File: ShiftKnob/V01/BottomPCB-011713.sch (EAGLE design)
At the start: 38 parts, among them IC2 7805DT, Q1 16MHz, Q2 MOSFET-NCHANNELSMD, Q3 MOSFET-NCHANNELSMD, Q4 MOSFET-NCHANNELSMD, Q5 MOSFET-NCHANNELSMD, Q6 MOSFET-NCHANNELSMD, U1 ATMEGA328

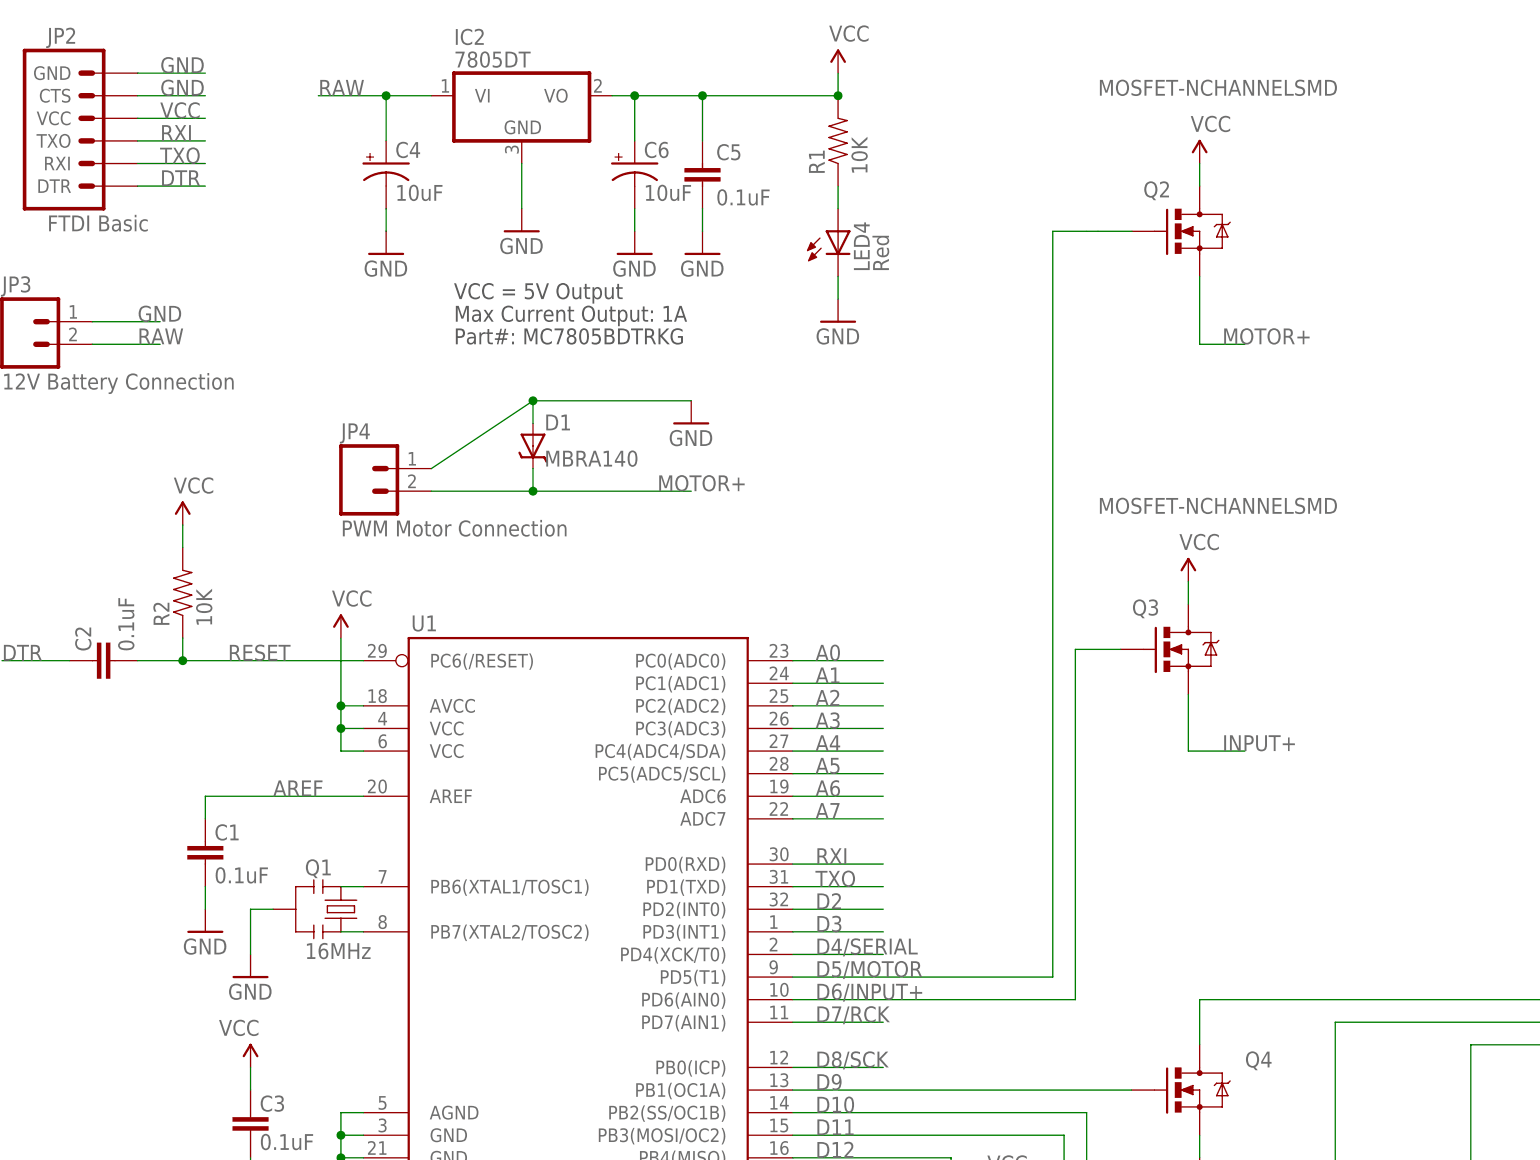
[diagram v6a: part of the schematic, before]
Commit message: add schottky diode to hand usb power auto selection
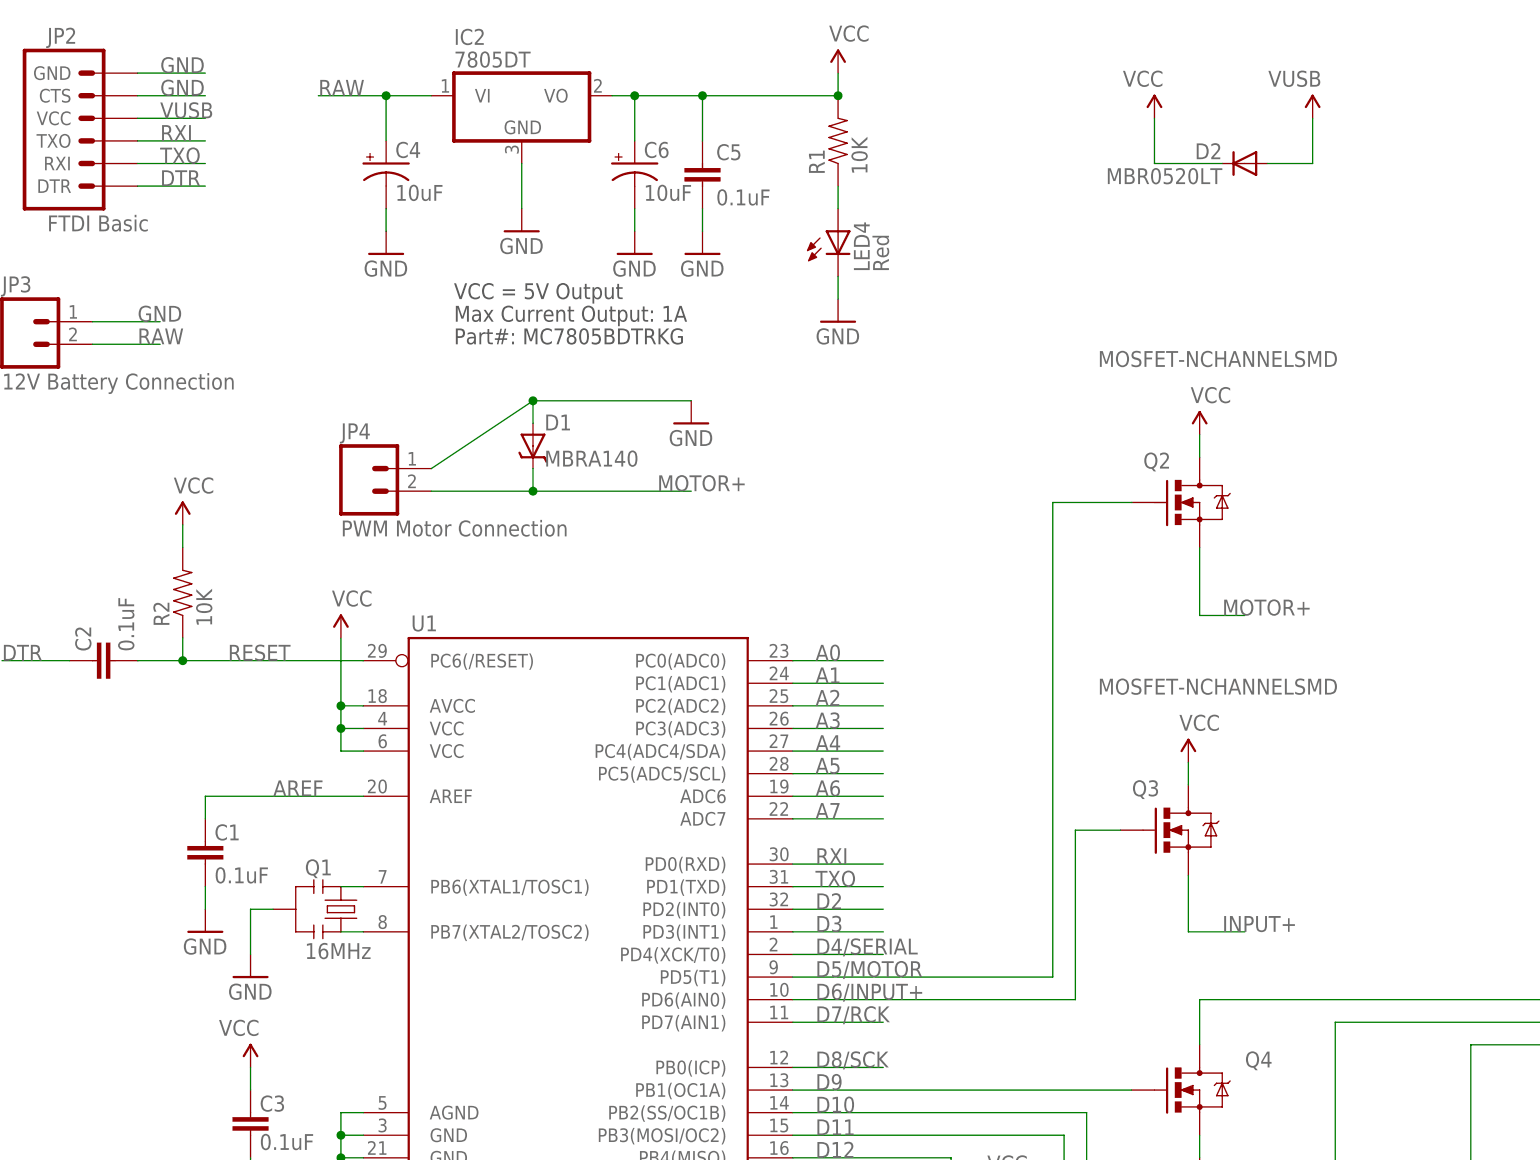
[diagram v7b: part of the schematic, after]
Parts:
- added D2: MBR0520LT, diode:MBR0520LT
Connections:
- new net VUSB: D2.A, JP2.VCC
- net VCC: now also D2.C; no longer JP2.VCC
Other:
- moved on the sheet: Q2, Q3
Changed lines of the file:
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@@
 <part name="P+2" library="SparkFun" deviceset="3.3V" device="" value="VCC"/>
 <part name="R12" library="SparkFun-Passives" deviceset="RESISTOR" device="0402-RES" value="10k"/>
+<part name="D2" library="diode" deviceset="MBR0520LT" device=""/>
+<part name="VUSB" library="SparkFun" deviceset="3.3V" device="" value="VUSB"/>
+<part name="VCC4" library="SparkFun" deviceset="3.3V" device="" value="VCC"/>
 </parts>
 <sheets>
@@
 <instance part="R8" gate="G$1" x="223.52" y="111.76" rot="R90"/>
 <instance part="R9" gate="G$1" x="231.14" y="109.22" rot="R90"/>
-<instance part="Q2" gate="G$1" x="144.78" y="180.34" smashed="yes">
-<attribute name="NAME" x="138.43" y="184.15" size="1.778" layer="95"/>
-<attribute name="VALUE" x="133.35" y="195.58" size="1.778" layer="96"/>
-</instance>
-<instance part="Q3" gate="G$1" x="143.51" y="133.35" smashed="yes">
-<attribute name="NAME" x="137.16" y="137.16" size="1.778" layer="95"/>
-<attribute name="VALUE" x="133.35" y="148.59" size="1.778" layer="96"/>
-</instance>
-<instance part="VCC1" gate="G$1" x="144.78" y="187.96"/>
-<instance part="VCC2" gate="G$1" x="143.51" y="140.97"/>
+<instance part="Q2" gate="G$1" x="144.78" y="149.86" smashed="yes">
+<attribute name="NAME" x="138.43" y="153.67" size="1.778" layer="95"/>
+<attribute name="VALUE" x="133.35" y="165.1" size="1.778" layer="96"/>
+</instance>
+<instance part="Q3" gate="G$1" x="143.51" y="113.03" smashed="yes">
+<attribute name="NAME" x="137.16" y="116.84" size="1.778" layer="95"/>
+<attribute name="VALUE" x="133.35" y="128.27" size="1.778" layer="96"/>
+</instance>
+<instance part="VCC1" gate="G$1" x="144.78" y="157.48"/>
+<instance part="VCC2" gate="G$1" x="143.51" y="120.65"/>
 <instance part="JP4" gate="G$1" x="50.8" y="151.13"/>
 <instance part="D1" gate="G$1" x="69.85" y="156.21" smashed="yes" rot="R270">
@@
 <attribute name="VALUE" x="125.73" y="61.722" size="1.778" layer="96" rot="R180"/>
 </instance>
+<instance part="D2" gate="G$1" x="149.86" y="187.96" rot="MR0"/>
+<instance part="VUSB" gate="G$1" x="157.48" y="193.04" rot="MR0"/>
+<instance part="VCC4" gate="G$1" x="139.7" y="193.04" rot="MR0"/>
 </instances>
 <busses>
@@
 <segment>
 <pinref part="Q3" gate="G$1" pin="S"/>
-<wire x1="143.51" y1="128.27" x2="143.51" y2="121.92" width="0.1524" layer="91"/>
-<wire x1="143.51" y1="121.92" x2="149.86" y2="121.92" width="0.1524" layer="91"/>
-<label x="147.32" y="121.92" size="1.778" layer="95"/>
+<wire x1="143.51" y1="107.95" x2="143.51" y2="101.6" width="0.1524" layer="91"/>
+<wire x1="143.51" y1="101.6" x2="149.86" y2="101.6" width="0.1524" layer="91"/>
+<label x="147.32" y="101.6" size="1.778" layer="95"/>
 </segment>
 </net>
@@
 <pinref part="U1" gate="G$1" pin="VCC@2"/>
 <pinref part="P+1" gate="G$1" pin="3.3V"/>
-</segment>
-<segment>
-<wire x1="25.4" y1="193.04" x2="33.02" y2="193.04" width="0.1524" layer="91"/>
-<label x="27.94" y="193.04" size="1.778" layer="95"/>
-<pinref part="JP2" gate="G$1" pin="VCC"/>
 </segment>
 <segment>
@@
 <segment>
 <pinref part="Q3" gate="G$1" pin="D"/>
-<wire x1="143.51" y1="138.43" x2="143.51" y2="140.97" width="0.1524" layer="91"/>
+<wire x1="143.51" y1="118.11" x2="143.51" y2="120.65" width="0.1524" layer="91"/>
 <pinref part="VCC2" gate="G$1" pin="3.3V"/>
 </segment>
 <segment>
 <pinref part="Q2" gate="G$1" pin="D"/>
-<wire x1="144.78" y1="185.42" x2="144.78" y2="187.96" width="0.1524" layer="91"/>
+<wire x1="144.78" y1="154.94" x2="144.78" y2="157.48" width="0.1524" layer="91"/>
 <pinref part="VCC1" gate="G$1" pin="3.3V"/>
 </segment>
@@
 <pinref part="P+2" gate="G$1" pin="3.3V"/>
 <wire x1="119.38" y1="71.12" x2="119.38" y2="68.58" width="0.1524" layer="91"/>
+</segment>
+<segment>
+<pinref part="D2" gate="G$1" pin="C"/>
+<wire x1="147.32" y1="187.96" x2="139.7" y2="187.96" width="0.1524" layer="91"/>
+<wire x1="139.7" y1="187.96" x2="139.7" y2="193.04" width="0.1524" layer="91"/>
+<pinref part="VCC4" gate="G$1" pin="3.3V"/>
 </segment>
 </net>
@@
 <pinref part="U1" gate="G$1" pin="PD5(T1)"/>
 <wire x1="99.06" y1="96.52" x2="128.27" y2="96.52" width="0.1524" layer="91"/>
-<wire x1="128.27" y1="96.52" x2="128.27" y2="180.34" width="0.1524" layer="91"/>
+<wire x1="128.27" y1="96.52" x2="128.27" y2="149.86" width="0.1524" layer="91"/>
 <pinref part="Q2" gate="G$1" pin="G"/>
-<wire x1="137.16" y1="180.34" x2="133.35" y2="180.34" width="0.1524" layer="91"/>
-<wire x1="133.35" y1="180.34" x2="132.08" y2="180.34" width="0.1524" layer="91"/>
-<wire x1="128.27" y1="180.34" x2="132.08" y2="180.34" width="0.1524" layer="91"/>
+<wire x1="128.27" y1="149.86" x2="137.16" y2="149.86" width="0.1524" layer="91"/>
 </segment>
 </net>
@@
 <pinref part="U1" gate="G$1" pin="PD6(AIN0)"/>
 <pinref part="Q3" gate="G$1" pin="G"/>
-<wire x1="135.89" y1="133.35" x2="130.81" y2="133.35" width="0.1524" layer="91"/>
+<wire x1="135.89" y1="113.03" x2="130.81" y2="113.03" width="0.1524" layer="91"/>
 <wire x1="99.06" y1="93.98" x2="130.81" y2="93.98" width="0.1524" layer="91"/>
-<wire x1="130.81" y1="93.98" x2="130.81" y2="133.35" width="0.1524" layer="91"/>
+<wire x1="130.81" y1="93.98" x2="130.81" y2="113.03" width="0.1524" layer="91"/>
 </segment>
 </net>
@@
 <segment>
 <pinref part="Q2" gate="G$1" pin="S"/>
-<wire x1="144.78" y1="175.26" x2="144.78" y2="167.64" width="0.1524" layer="91"/>
-<wire x1="144.78" y1="167.64" x2="149.86" y2="167.64" width="0.1524" layer="91"/>
-<label x="147.32" y="167.64" size="1.778" layer="95"/>
+<wire x1="144.78" y1="144.78" x2="144.78" y2="137.16" width="0.1524" layer="91"/>
+<wire x1="144.78" y1="137.16" x2="149.86" y2="137.16" width="0.1524" layer="91"/>
+<label x="147.32" y="137.16" size="1.778" layer="95"/>
 </segment>
 <segment>
@@
 </segment>
 </net>
+<net name="VUSB" class="0">
+<segment>
+<wire x1="25.4" y1="193.04" x2="33.02" y2="193.04" width="0.1524" layer="91"/>
+<label x="27.94" y="193.04" size="1.778" layer="95"/>
+<pinref part="JP2" gate="G$1" pin="VCC"/>
+</segment>
+<segment>
+<pinref part="D2" gate="G$1" pin="A"/>
+<wire x1="152.4" y1="187.96" x2="157.48" y2="187.96" width="0.1524" layer="91"/>
+<wire x1="157.48" y1="187.96" x2="157.48" y2="193.04" width="0.1524" layer="91"/>
+<pinref part="VUSB" gate="G$1" pin="3.3V"/>
+</segment>
+</net>
